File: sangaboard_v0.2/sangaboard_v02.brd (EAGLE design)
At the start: 67.3 x 55.5 mm, 23 parts, among them IC1 ULN2003A, IC2 ULN2003A

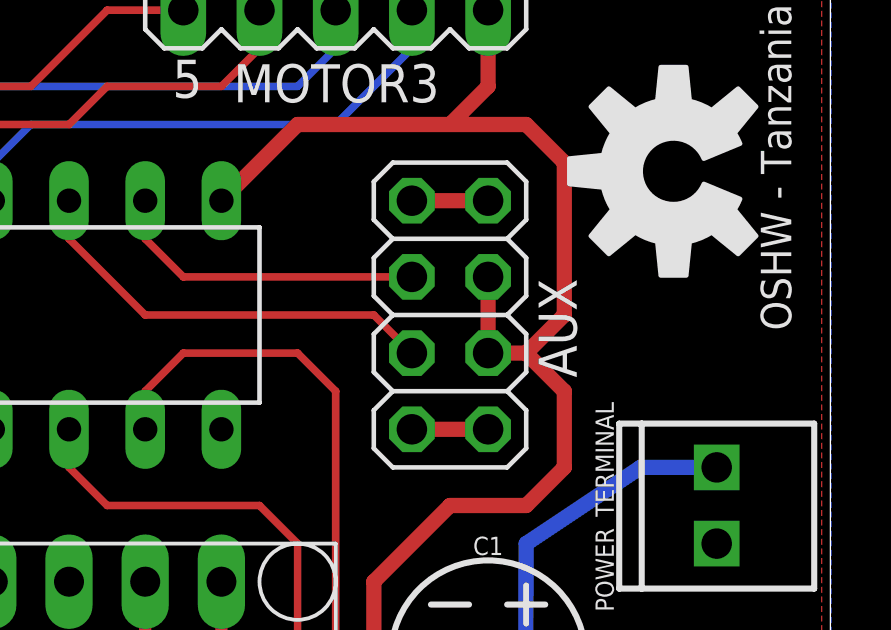
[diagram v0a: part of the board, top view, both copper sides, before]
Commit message: Updated Bottom Layer
Have updated the Aux header pin connection to Ground.
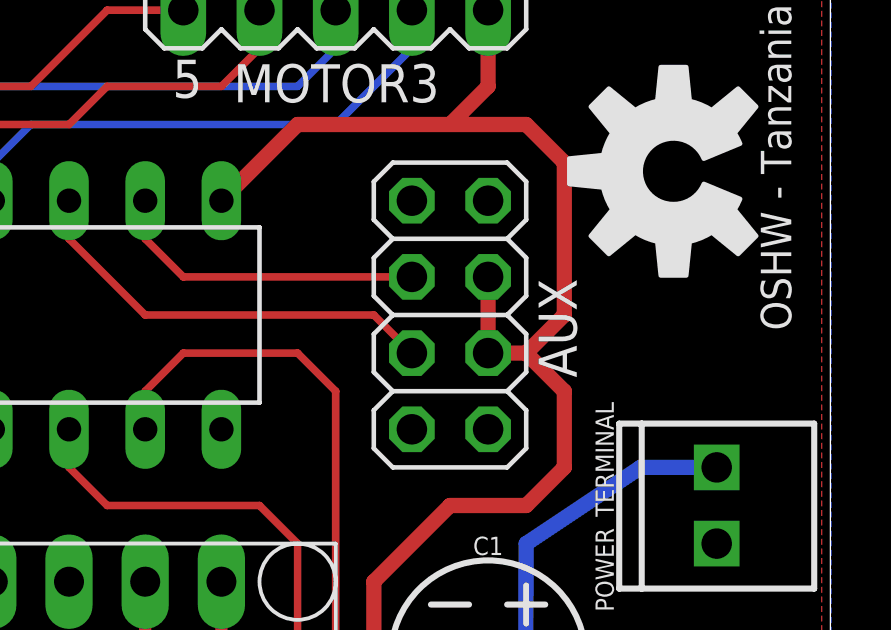
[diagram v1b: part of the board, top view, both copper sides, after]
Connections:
- removed net L1: AUX.1, AUX.2
- removed net L2: AUX.7, AUX.8
- net GND: now also AUX.1, AUX.2, AUX.7, AUX.8
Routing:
- net L2: track 2.54 -> 0.00 mm
- net L1: track 2.54 -> 0.00 mm
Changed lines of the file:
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@@
 <?xml version="1.0" encoding="utf-8"?>
 <!DOCTYPE eagle SYSTEM "eagle.dtd">
-<eagle version="8.6.0">
+<eagle version="9.0.0">
 <drawing>
 <settings>
@@
 <wire x1="64.0606" y1="14.7706" x2="64.59" y2="15.3" width="0.254" layer="1"/>
 <wire x1="60" y1="16" x2="61.2294" y2="14.7706" width="0.254" layer="1"/>
+<contactref element="AUX" pad="1"/>
+<contactref element="AUX" pad="7"/>
+<contactref element="AUX" pad="2"/>
+<contactref element="AUX" pad="8"/>
 </signal>
 <signal name="VIN">
@@
 <wire x1="47.71" y1="10.71" x2="47.71" y2="10.71" width="0.4064" layer="16"/>
 </signal>
-<signal name="L1">
-<contactref element="AUX" pad="1"/>
-<contactref element="AUX" pad="2"/>
-<wire x1="53.34" y1="41.91" x2="55.88" y2="41.91" width="0.508" layer="1"/>
-</signal>
-<signal name="L2">
-<contactref element="AUX" pad="7"/>
-<contactref element="AUX" pad="8"/>
-<wire x1="53.34" y1="34.29" x2="55.88" y2="34.29" width="0.508" layer="1"/>
-</signal>
 <signal name="3V3">
